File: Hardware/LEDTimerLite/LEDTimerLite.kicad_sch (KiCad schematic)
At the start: 27 parts, among them J1 Program, J2 LED, J3 PWR, Q1 S8050, SW1 SW_Push, SW4 SW_PWR, U1 AP7383-36WW7, U2 PIC16LF18326, U4 BCR_421U_E6327, Y1 32.768 kHz

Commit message: LTL: try new PCB layout
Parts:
- added D2: Red LED, LED_SMD:LED_0805_2012Metric_Pad1.15x1.40mm_HandSolder, symbol Device:LED
- added R4: 560, Resistor_SMD:R_0805_2012Metric_Pad1.20x1.40mm_HandSolder, symbol Device:R
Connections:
- net GND: now also R4.2
- net LED: now reaches U2.8 (RC1)
- net LED: now also D2.2 (A)
- new net: D2.1 (K), R4.1
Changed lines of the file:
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@@
+	)
+	(junction
+		(at 241.3 111.76)
+		(diameter 0)
+		(color 0 0 0 0)
 	)
 	(junction
@@
 	(wire
 		(pts
+			(xy 241.3 100.33) (xy 241.3 111.76)
+		)
+		(stroke
+			(width 0)
+			(type default)
+		)
+	)
+	(wire
+		(pts
 			(xy 116.205 106.68) (xy 116.205 128.27)
 		)
@@
 	(wire
 		(pts
+			(xy 218.44 100.33) (xy 220.98 100.33)
+		)
+		(stroke
+			(width 0)
+			(type default)
+		)
+	)
+	(wire
+		(pts
 			(xy 193.04 140.97) (xy 194.31 140.97)
 		)
@@
 	(wire
 		(pts
+			(xy 208.28 114.3) (xy 208.28 100.33)
+		)
+		(stroke
+			(width 0)
+			(type default)
+		)
+	)
+	(wire
+		(pts
 			(xy 167.64 101.6) (xy 167.64 124.46)
 		)
@@
 	(wire
 		(pts
+			(xy 165.1 114.3) (xy 208.28 114.3)
+		)
+		(stroke
+			(width 0)
+			(type default)
+		)
+	)
+	(wire
+		(pts
 			(xy 66.04 34.29) (xy 66.04 36.83)
 		)
@@
 	(wire
 		(pts
+			(xy 208.28 100.33) (xy 210.82 100.33)
+		)
+		(stroke
+			(width 0)
+			(type default)
+		)
+	)
+	(wire
+		(pts
 			(xy 197.485 139.7) (xy 198.755 139.7)
 		)
@@
 	(wire
 		(pts
+			(xy 228.6 100.33) (xy 241.3 100.33)
+		)
+		(stroke
+			(width 0)
+			(type default)
+		)
+	)
+	(wire
+		(pts
 			(xy 103.505 101.6) (xy 134.62 101.6)
 		)
@@
 			(width 0)
 			(type default)
+		)
+	)
+	(label "LED"
+		(at 170.18 114.3 0)
+		(fields_autoplaced yes)
+		(effects
+			(font
+				(size 1.27 1.27)
+			)
+			(justify left bottom)
 		)
 	)
@@
 	(symbol
 		(lib_id "Device:R")
+		(at 224.79 100.33 90)
+		(unit 1)
+		(exclude_from_sim no)
+		(in_bom yes)
+		(on_board yes)
+		(dnp no)
+		(fields_autoplaced yes)
+		(property "Reference" "R4"
+			(at 224.79 93.98 90)
+			(effects
+				(font
+					(size 1.27 1.27)
+				)
+			)
+		)
+		(property "Value" "560"
+			(at 224.79 96.52 90)
+			(effects
+				(font
+					(size 1.27 1.27)
+				)
+			)
+		)
+		(property "Footprint" "Resistor_SMD:R_0805_2012Metric_Pad1.20x1.40mm_HandSolder"
+			(at 224.79 102.108 90)
+			(effects
+				(font
+					(size 1.27 1.27)
+				)
+				(hide yes)
+			)
+		)
+		(property "Datasheet" "~"
+			(at 224.79 100.33 0)
+			(effects
+				(font
+					(size 1.27 1.27)
+				)
+				(hide yes)
+			)
+		)
+		(property "Description" "Resistor"
+			(at 224.79 100.33 0)
+			(effects
+				(font
+					(size 1.27 1.27)
+				)
+				(hide yes)
+			)
+		)
+		(pin "1"
+		)
+		(pin "2"
+		)
+		(instances
+			(project ""
+				(path "/9e18dfcf-a5f4-466f-a700-bf8a16e1e469"
+					(reference "R4")
+					(unit 1)
+				)
+			)
+		)
+	)
+	(symbol
+		(lib_id "Device:R")
 		(at 132.08 140.97 0)
 		(unit 1)
@@
 					(unit 1)
 				)
+			)
+		)
+	)
+	(symbol
+		(lib_id "Device:LED")
+		(at 214.63 100.33 180)
+		(unit 1)
+		(exclude_from_sim no)
+		(in_bom yes)
+		(on_board yes)
+		(dnp no)
+		(fields_autoplaced yes)
+		(property "Reference" "D2"
+			(at 216.2175 92.71 0)
+			(effects
+				(font
+					(size 1.27 1.27)
+				)
+			)
+		)
+		(property "Value" "Red LED"
+			(at 216.2175 95.25 0)
+			(effects
+				(font
+					(size 1.27 1.27)
+				)
+			)
+		)
+		(property "Footprint" "LED_SMD:LED_0805_2012Metric_Pad1.15x1.40mm_HandSolder"
+			(at 214.63 100.33 0)
+			(effects
+				(font
+					(size 1.27 1.27)
+				)
+				(hide yes)
+			)
+		)
+		(property "Datasheet" "~"
+			(at 214.63 100.33 0)
+			(effects
+				(font
+					(size 1.27 1.27)
+				)
+				(hide yes)
+			)
+		)
+		(property "Description" "Light emitting diode"
+			(at 214.63 100.33 0)
+			(effects
+				(font
+					(size 1.27 1.27)
+				)
+				(hide yes)
+			)
+		)
+		(pin "1"
+		)
+		(pin "2"
+		)
+		(instances
+			(project ""
+				(path "/9e18dfcf-a5f4-466f-a700-bf8a16e1e469"
+					(reference "D2")
+					(unit 1)
+				)

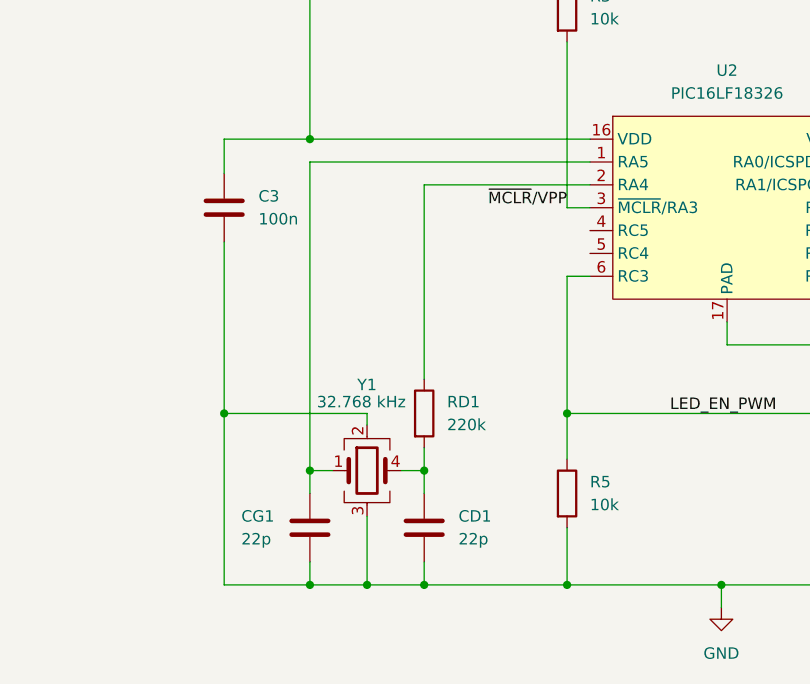
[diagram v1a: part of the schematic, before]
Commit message: LTL: improve track routing
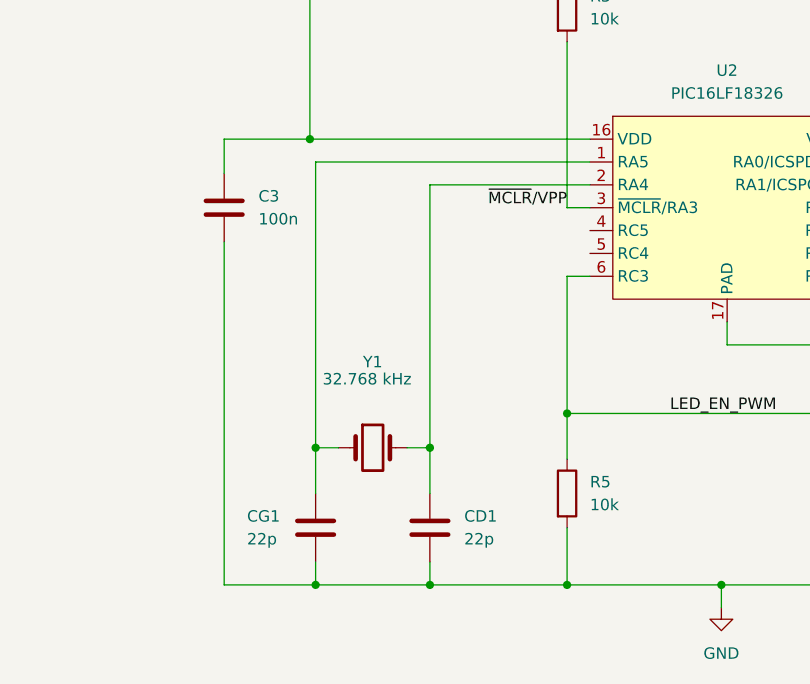
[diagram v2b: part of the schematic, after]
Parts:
- removed RD1: 220k, Resistor_SMD:R_0805_2012Metric_Pad1.20x1.40mm_HandSolder, symbol Device:R
- Y1: footprint Crystal:Crystal_SMD_Abracon_ABS25-4Pin_8.0x3.8mm -> Crystal:Crystal_SMD_MicroCrystal_CC8V-T1A-2Pin_2.0x1.2mm_HandSoldering; symbol Device:Crystal_GND23 -> Device:Crystal
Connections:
- net GND: no longer Y1.2, Y1.3
- net at CD1.1: now also U2.2 (RA4), Y1.2; no longer Y1.4
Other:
- moved on the sheet: CD1, CG1

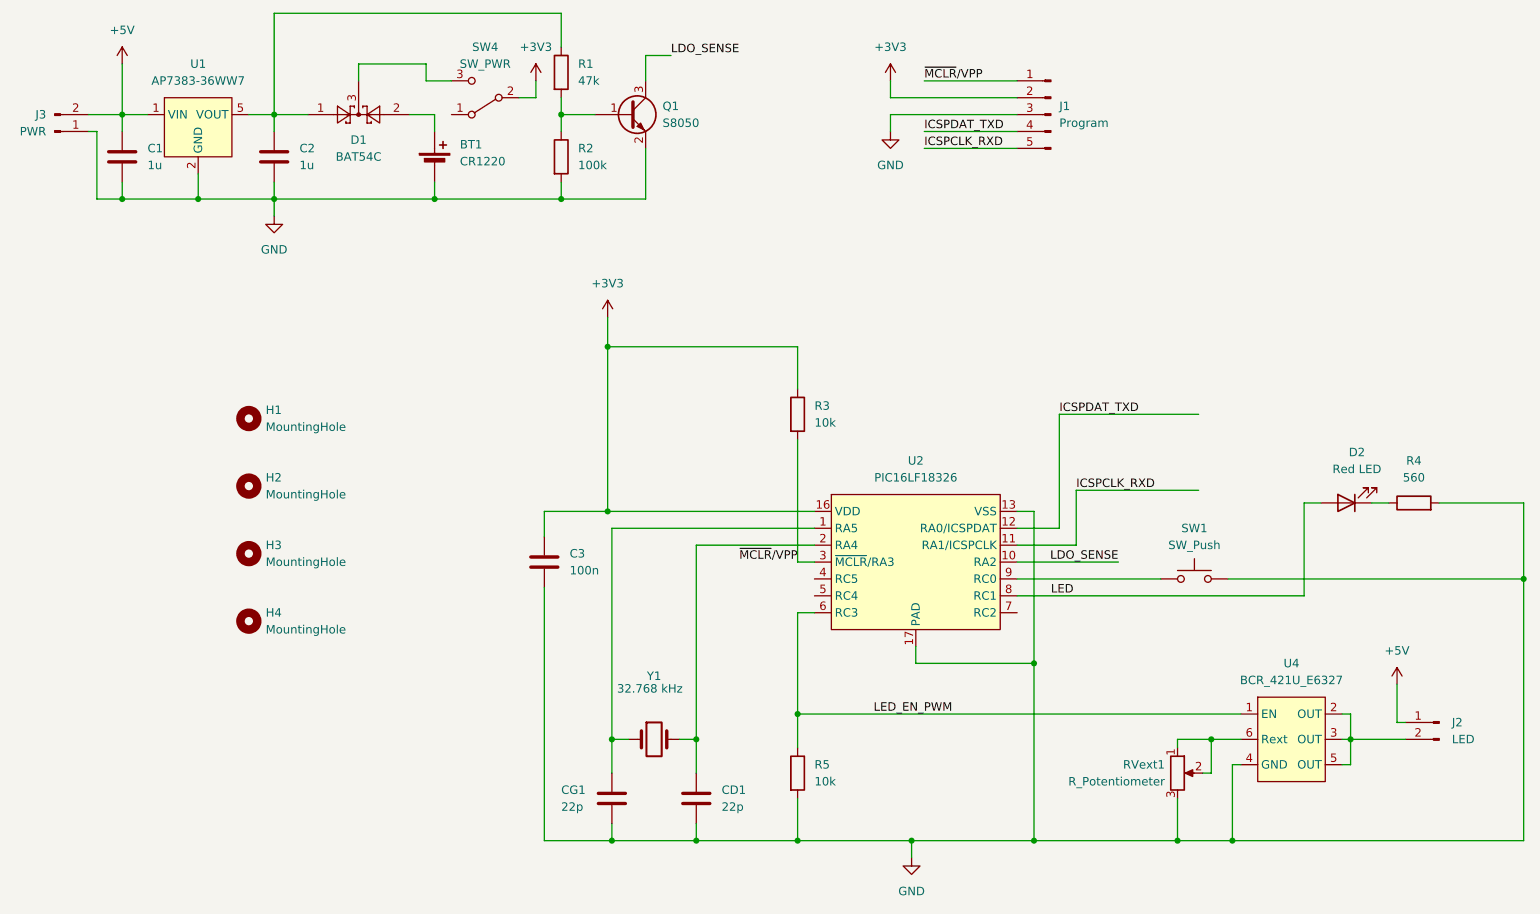
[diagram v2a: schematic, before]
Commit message: LTL: replace BAT54C with 1SS384 (lower Vf)
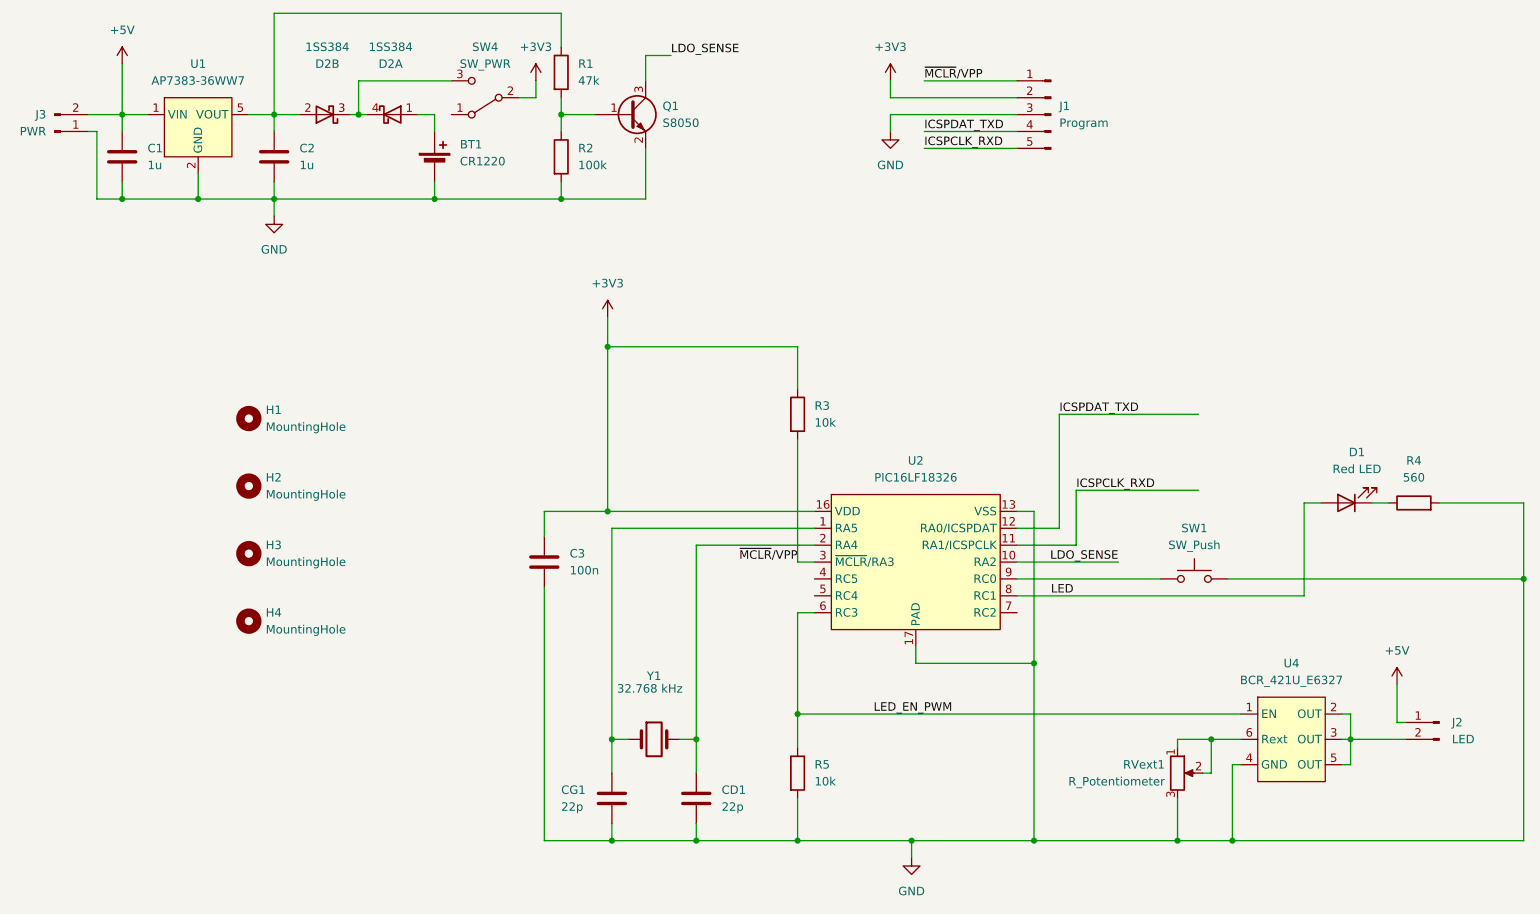
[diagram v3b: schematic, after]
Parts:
- removed D1: BAT54C, Package_TO_SOT_SMD:SOT-416, symbol Diode:BAT54C
- added D2: 1SS384, Package_TO_SOT_SMD:SOT-343_SC-70-4, symbol LEDTimer:1SS384
- renumbered D2 to D1
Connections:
- net at C2.1, R1.1, U1.5 (VOUT): now also D2.2 (A)
- net at BT1.1 (+): now also D2.1 (A)
- net at SW4.3 (C): now also D2.3 (K), D2.4 (K)

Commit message: LTL: fix ERC issues
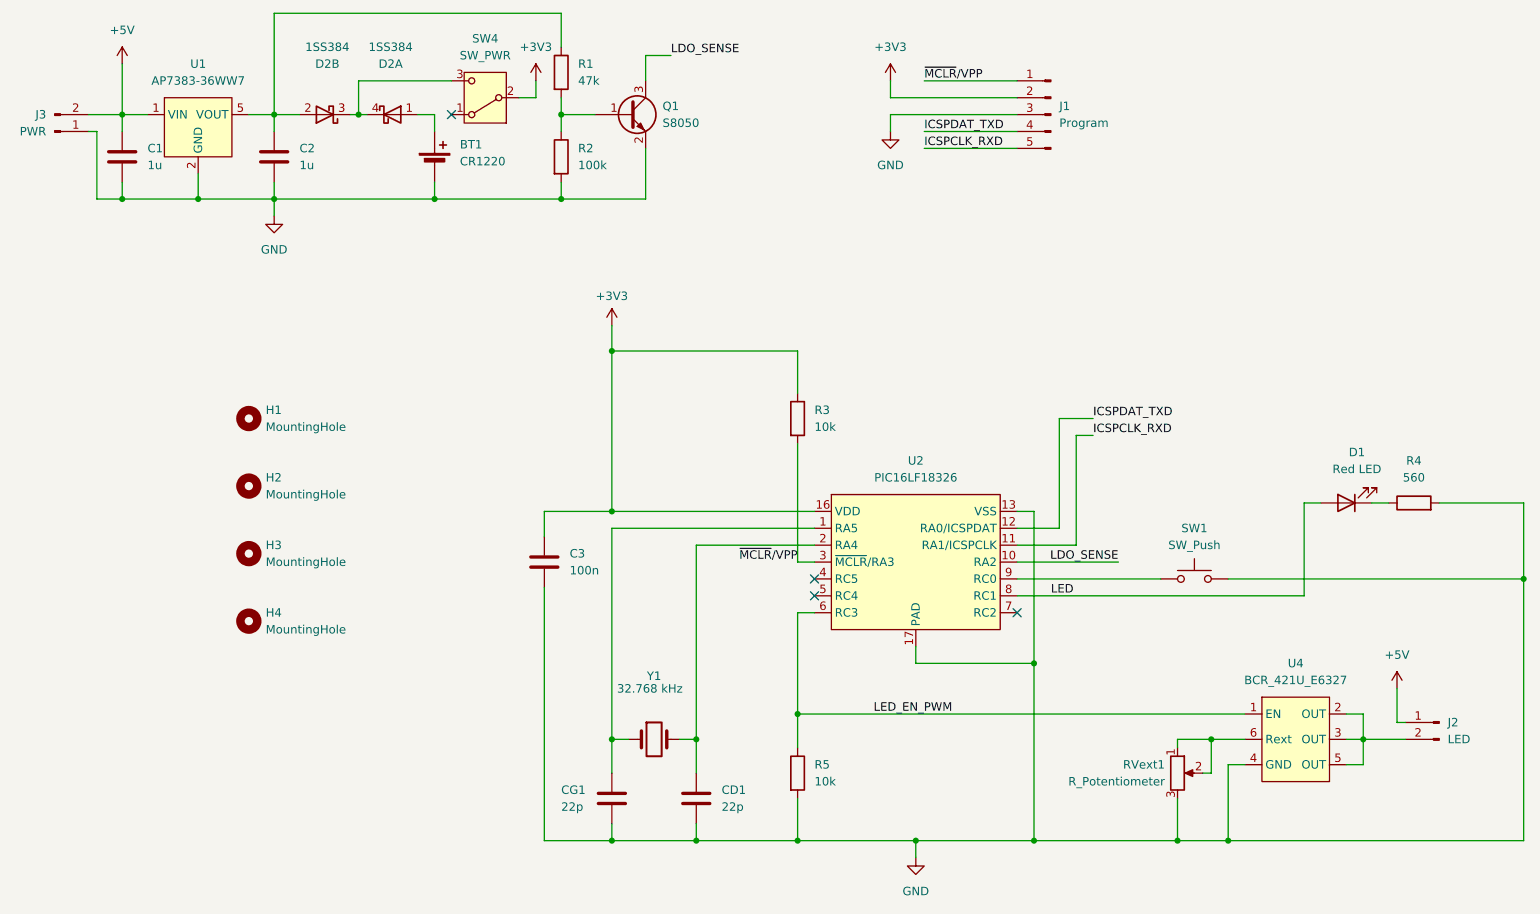
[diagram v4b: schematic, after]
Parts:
- J2, J3: symbol Connector:Conn_01x02_Male -> Connector:Conn_01x02_Pin
- U2: symbol LEDTimer:PIC16F1825 -> LEDTimer:PIC16LF18326
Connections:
- no-connect marks 0 -> 4
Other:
- moved on the sheet: R3, U4

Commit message: LTL: add extra test points, optimize layout
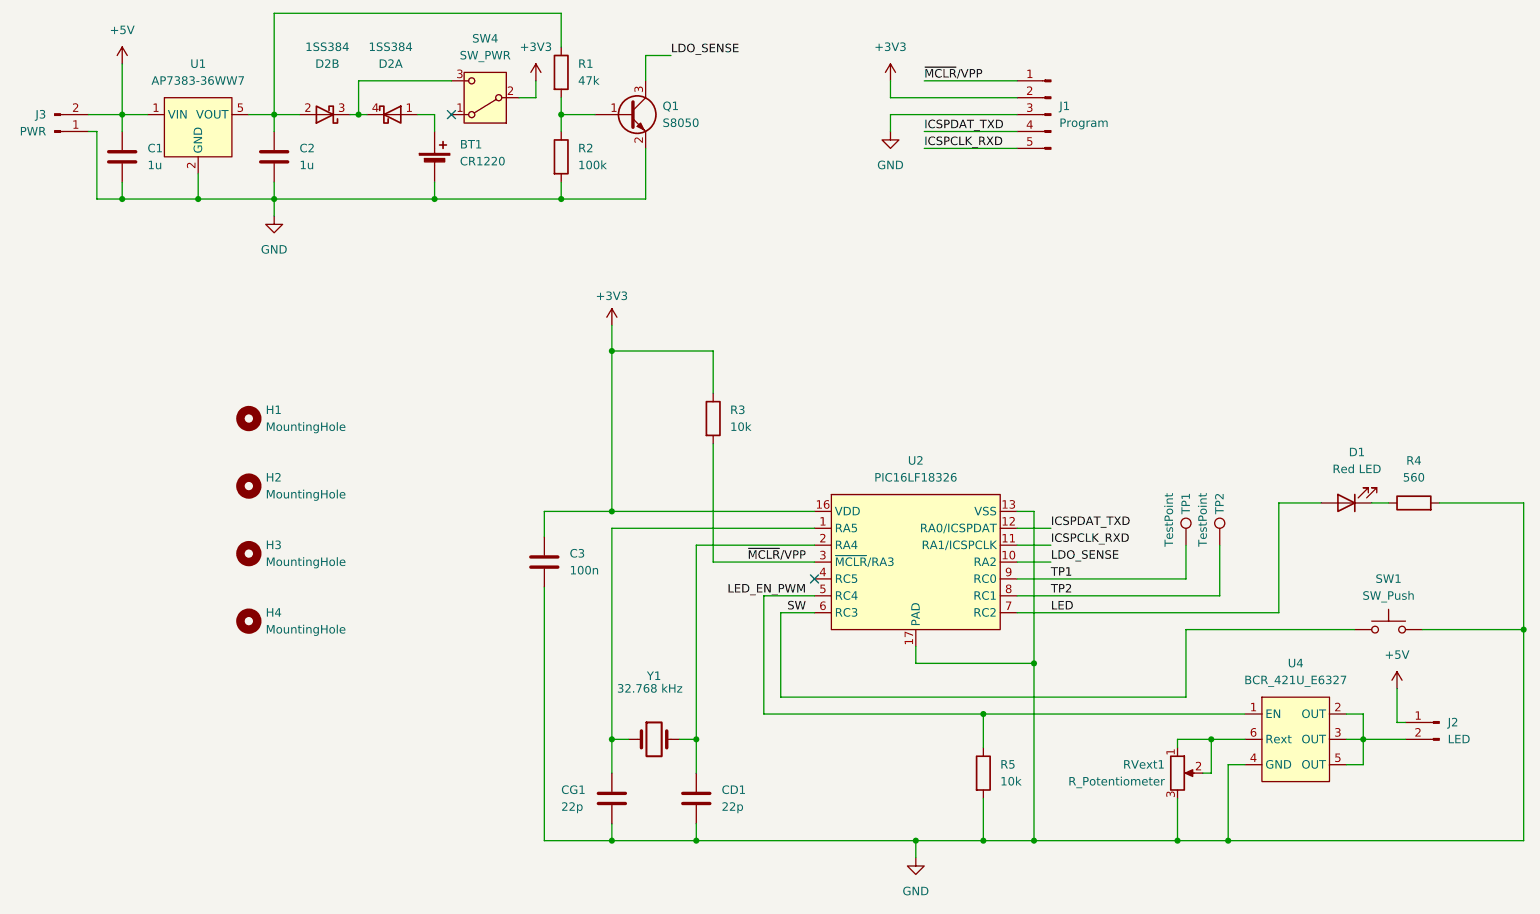
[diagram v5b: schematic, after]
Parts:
- added TP1, TP2: TestPoint, TestPoint:TestPoint_Pad_D1.5mm, symbol Connector:TestPoint
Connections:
- net LED: now also U2.7 (RC2); no longer U2.8 (RC1)
- net LED_EN_PWM: now also U2.5 (RC4); no longer U2.6 (RC3)
- net SW: now reaches SW1.2
- net SW: now also U2.6 (RC3); no longer U2.9 (RC0)
- new net TP1: TP1.1, U2.9 (RC0)
- new net TP2: TP2.1, U2.8 (RC1)
- no-connect marks 4 -> 2
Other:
- moved on the sheet: R3, R5, SW1

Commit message: LTL: replace LED driver and RVext1
Use BCR321U (250 mA) instead of BCR421U (150 mA).
Use TC33X-2-101E as RVext1 because it's cheaper.
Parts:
- RVext1: footprint Potentiometer_SMD:Potentiometer_Vishay_TS53YJ_Vertical -> Potentiometer_SMD:Potentiometer_Bourns_TC33X_Vertical
- U4: value BCR_421U_E6327 -> BCR_321U_E6327
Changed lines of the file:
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@@
 			)
 		)
-		(property "Footprint" "Potentiometer_SMD:Potentiometer_Vishay_TS53YJ_Vertical"
+		(property "Footprint" "Potentiometer_SMD:Potentiometer_Bourns_TC33X_Vertical"
 			(at 189.23 140.97 0)
 			(effects
@@
 			)
 		)
-		(property "Value" "BCR_421U_E6327"
+		(property "Value" "BCR_321U_E6327"
 			(at 207.01 127 0)
 			(effects
@@
 			)
 		)
-		(property "Datasheet" "https://4donline.ihs.com/images/VipMasterIC/IC/INFN/INFN-S-A0000798853/INFN-S-A0000798853-1.pdf?hkey=6D3A4C79FDBF58556ACFDE234799DDF0"
+		(property "Datasheet" "https://www.infineon.com/dgdl/Infineon-BCR320U_BCR321U-DataSheet-v02_02-EN.pdf?fileId=5546d4624b0b249c014b7d69949b463b"
 			(at 207.01 152.4 0)
 			(effects

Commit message: LTL: add debouncing capacitor to SW
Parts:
- added C4: 100n, Capacitor_SMD:C_0805_2012Metric_Pad1.18x1.45mm_HandSolder, symbol Device:C
- U1: value AP7383-36WW7 -> AP7383-33WW7
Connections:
- net GND: now also C4.2
- net SW: now also C4.1
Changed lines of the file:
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@@
+	)
+	(junction
+		(at 129.54 151.13)
+		(diameter 0)
+		(color 0 0 0 0)
 	)
 	(junction
@@
 	)
 	(junction
+		(at 129.54 129.54)
+		(diameter 0)
+		(color 0 0 0 0)
+	)
+	(junction
 		(at 196.85 151.13)
 		(diameter 0)
@@
 	(wire
 		(pts
+			(xy 129.54 151.13) (xy 149.86 151.13)
+		)
+		(stroke
+			(width 0)
+			(type default)
+		)
+	)
+	(wire
+		(pts
 			(xy 116.84 135.89) (xy 116.84 140.97)
 		)
@@
 	(wire
 		(pts
-			(xy 116.84 151.13) (xy 149.86 151.13)
+			(xy 116.84 151.13) (xy 129.54 151.13)
 		)
 		(stroke
@@
 	(wire
 		(pts
+			(xy 129.54 129.54) (xy 129.54 140.97)
+		)
+		(stroke
+			(width 0)
+			(type default)
+		)
+	)
+	(wire
+		(pts
 			(xy 160.02 144.78) (xy 160.02 151.13)
 		)
@@
 		(pts
 			(xy 30.48 41.91) (xy 30.48 44.45)
+		)
+		(stroke
+			(width 0)
+			(type default)
+		)
+	)
+	(wire
+		(pts
+			(xy 129.54 148.59) (xy 129.54 151.13)
 		)
 		(stroke
@@
 	)
 	(symbol
+		(lib_id "Device:C")
+		(at 129.54 144.78 0)
+		(unit 1)
+		(exclude_from_sim no)
+		(in_bom yes)
+		(on_board yes)
+		(dnp no)
+		(fields_autoplaced yes)
+		(property "Reference" "C4"
+			(at 133.35 143.5099 0)
+			(effects
+				(font
+					(size 1.27 1.27)
+				)
+				(justify left)
+			)
+		)
+		(property "Value" "100n"
+			(at 133.35 146.0499 0)
+			(effects
+				(font
+					(size 1.27 1.27)
+				)
+				(justify left)
+			)
+		)
+		(property "Footprint" "Capacitor_SMD:C_0805_2012Metric_Pad1.18x1.45mm_HandSolder"
+			(at 130.5052 148.59 0)
+			(effects
+				(font
+					(size 1.27 1.27)
+				)
+				(hide yes)
+			)
+		)
+		(property "Datasheet" "~"
+			(at 129.54 144.78 0)
+			(effects
+				(font
+					(size 1.27 1.27)
+				)
+				(hide yes)
+			)
+		)
+		(property "Description" ""
+			(at 129.54 144.78 0)
+			(effects
+				(font
+					(size 1.27 1.27)
+				)
+				(hide yes)
+			)
+		)
+		(pin "1"
+		)
+		(pin "2"
+		)
+		(instances
+			(project "LEDTimerLite"
+				(path "/9e18dfcf-a5f4-466f-a700-bf8a16e1e469"
+					(reference "C4")
+					(unit 1)
+				)
+			)
+		)
+	)
+	(symbol
 		(lib_id "Connector:Conn_01x02_Pin")
 		(at 228.6 133.35 0)
@@
 			)
 		)
-		(property "Value" "AP7383-36WW7"
+		(property "Value" "AP7383-33WW7"
 			(at 41.91 36.83 0)
 			(effects
